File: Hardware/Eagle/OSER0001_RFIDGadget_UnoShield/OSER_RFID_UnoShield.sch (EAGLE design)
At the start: 6 parts, among them U1 ARDUINOR3-BPLACE

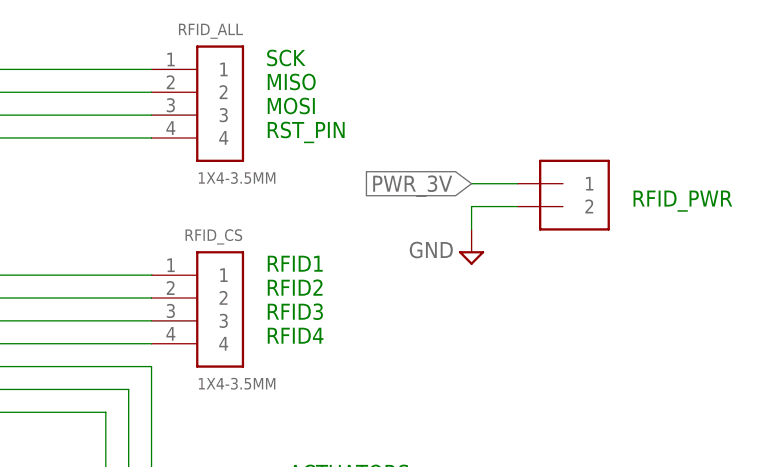
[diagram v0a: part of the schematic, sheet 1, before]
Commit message: Changed to 5V for RFID Readers
Switched to the PN532 RFID reader which uses 5V.
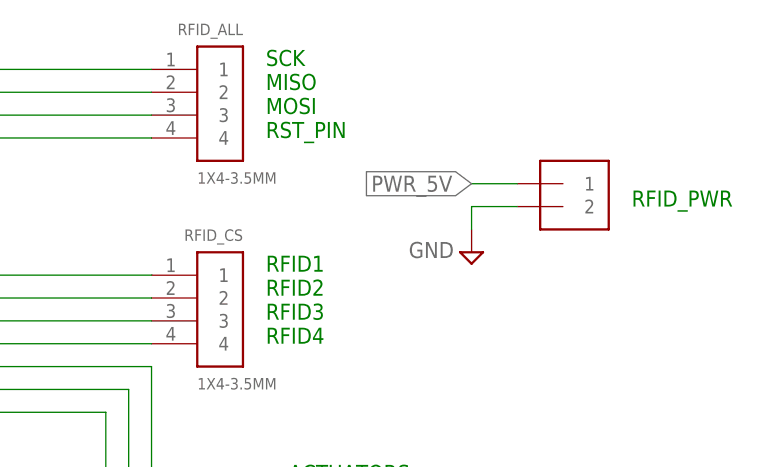
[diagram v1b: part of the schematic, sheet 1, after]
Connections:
- net PWR_3V: no longer RFID_PWR.1
- net PWR_5V: now also RFID_PWR.1
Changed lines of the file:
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@@
 <label x="48.26" y="-7.62" size="1.778" layer="95" rot="R270" xref="yes"/>
-</segment>
-<segment>
-<pinref part="RFID_PWR" gate="G$1" pin="1"/>
-<wire x1="147.32" y1="86.36" x2="142.24" y2="86.36" width="0.1524" layer="91"/>
-<label x="142.24" y="86.36" size="1.778" layer="95" rot="R180" xref="yes"/>
 </segment>
 </net>
@@
 <wire x1="109.22" y1="40.64" x2="106.68" y2="40.64" width="0.1524" layer="91"/>
 <label x="106.68" y="40.64" size="1.778" layer="95" rot="R180" xref="yes"/>
+</segment>
+<segment>
+<pinref part="RFID_PWR" gate="G$1" pin="1"/>
+<wire x1="147.32" y1="86.36" x2="142.24" y2="86.36" width="0.1524" layer="91"/>
+<label x="142.24" y="86.36" size="1.778" layer="95" rot="R180" xref="yes"/>
 </segment>
 </net>
@@
 </sheet>
 </sheets>
+<errors>
+</errors>
 </schematic>
 </drawing>
